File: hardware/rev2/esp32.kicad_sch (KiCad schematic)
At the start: 0 parts

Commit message: Begun ESP32 Power + Antenna
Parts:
- added C20: 10 uF, symbol Device:C
- added C21, C22, C24, C25, C26: 0,1 uF, symbol Device:C
- added C23, C27, C28: 1 uF, symbol Device:C
- added C29: 10 nF, symbol Device:C
- added C30, C31, C32, C33: TBD, symbol Device:C
- added L7: 2,0 nH (0,1 nH), symbol Device:L
- added L8, L9: TBD, symbol Device:L
- added U3: ESP32-S3, Package_DFN_QFN:QFN-56-1EP_7x7mm_P0.4mm_EP4x4mm, symbol MCU_Espressif:ESP32-S3
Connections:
- new net: C21.1, L7.2, U3.2 (VDD3P3), U3.3 (VDD3P3)
- new net: C31.1, C32.1, L8.1, L9.2
- new net: C30.1, L8.2, U3.1 (LNA_IN)
- new net Antenn (ESD mellan?): C33.1, L9.1
- new net BUSY: U3.18 (GPIO13)
- new net CS: U3.14 (GPIO9)
- new net DIO1: U3.17 (GPIO12)
- new net GND: C20.2, C21.2, C22.2, C23.2, C24.2, C25.2, C26.2, C27.2, C28.2, C29.2, C30.2, C31.2, C32.2, C33.2, U3.57 (GND)
- new net MISO: U3.12 (GPIO7)
- new net MOSI: U3.13 (GPIO8)
- new net Reset: U3.16 (GPIO11)
- new net SCK: U3.15 (GPIO10)
- new net VDD33: C20.1, C22.1, C23.1, C24.1, C25.1, C28.1, C29.1, L7.1, U3.20 (VDD3P3_RTC), U3.46 (VDD3P3_CPU), U3.55 (VDDA), U3.56 (VDDA)
- new net VDD_SPI: C26.1, C27.1, U3.29 (VDD_SPI)
- no-connect marks 0 -> 5

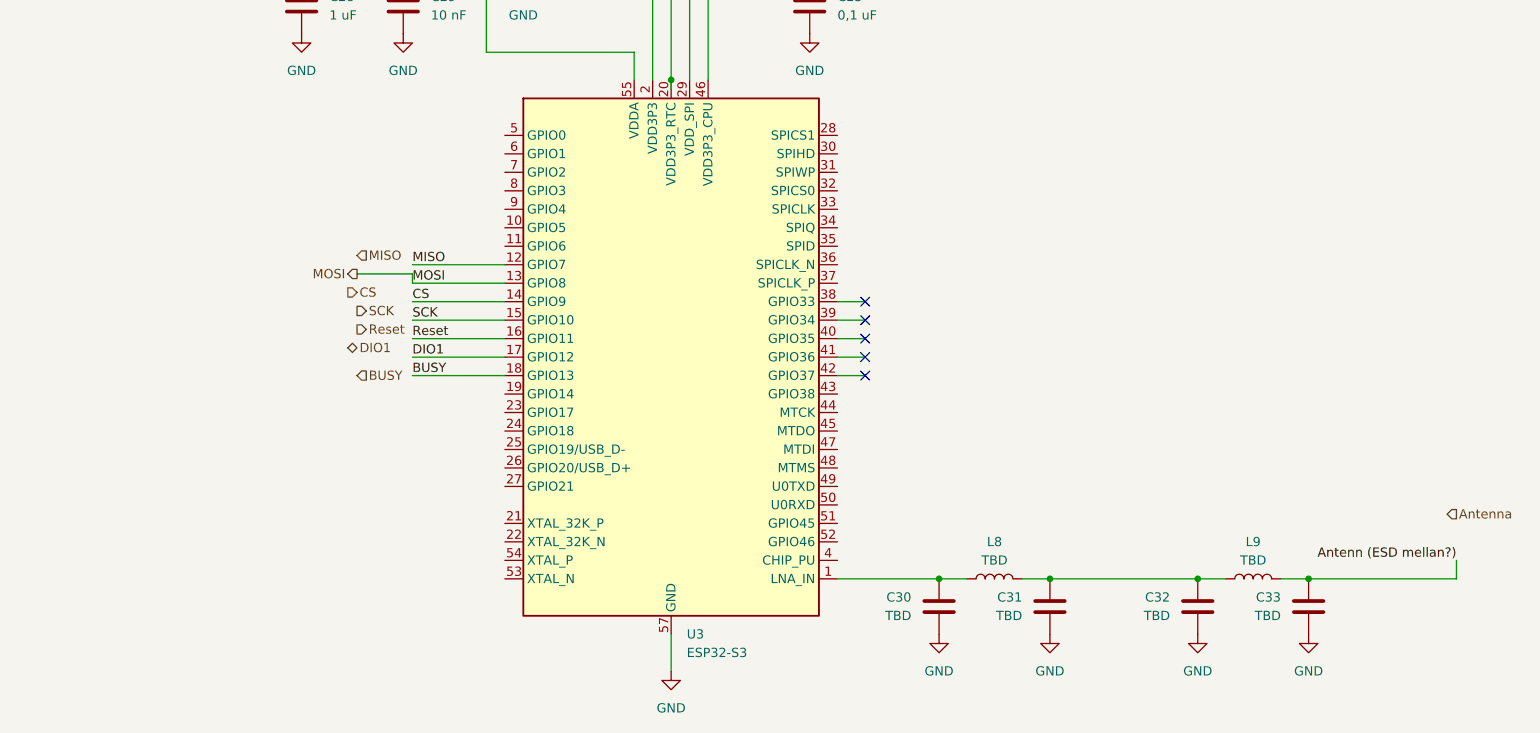
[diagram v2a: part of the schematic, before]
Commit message: added USB port to ESP32
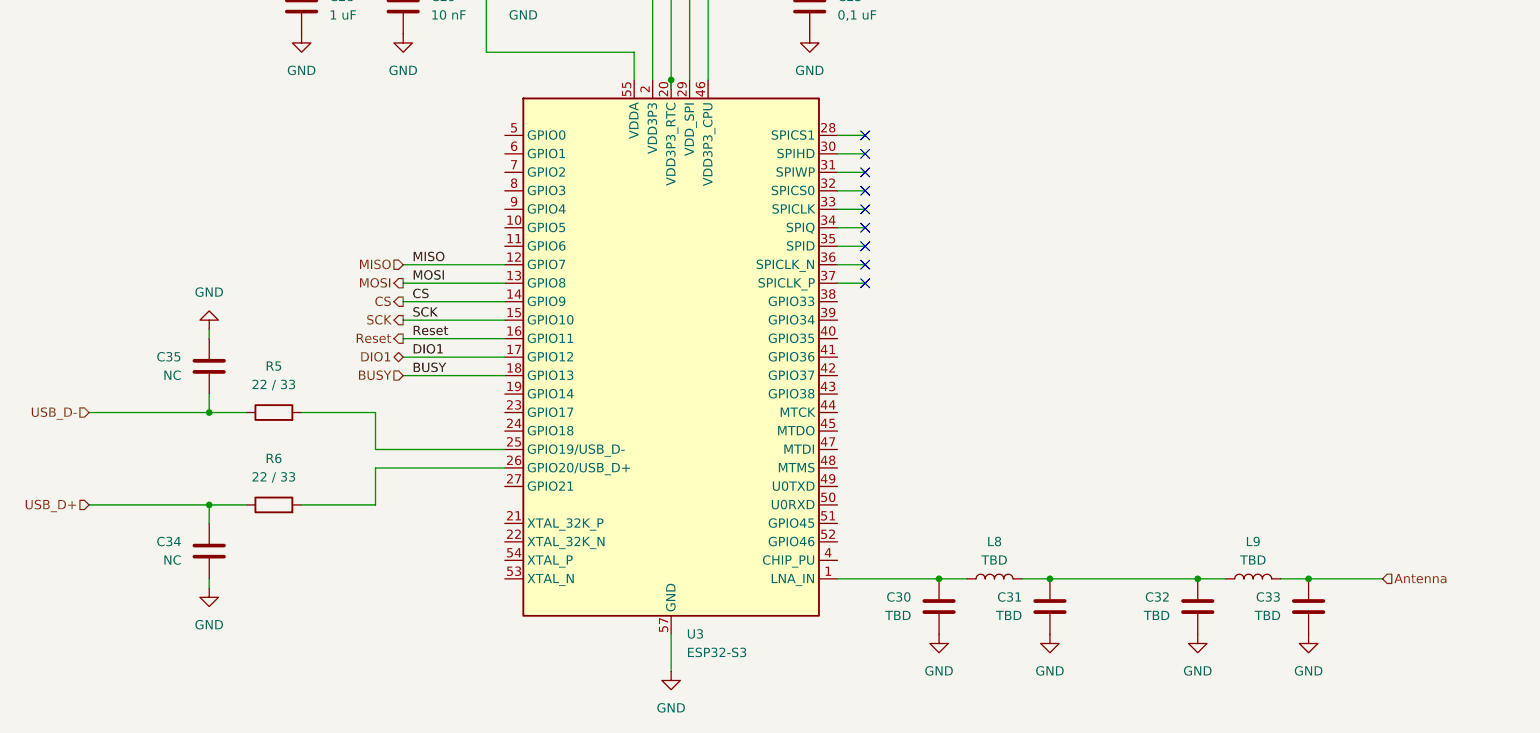
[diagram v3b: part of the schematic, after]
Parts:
- added C34, C35: NC, symbol Device:C
- added R5, R6: 22 / 33, symbol Device:R
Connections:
- net Antenn (ESD mellan?) is gone; now on net Antenna: C33.1, L9.1
- net GND: now also C34.2, C35.2
- net at U3.25 (GPIO19/USB_D-): now also R5.2
- net at U3.26 (GPIO20/USB_D+): now also R6.2
- new net USB_D+: C34.1, R6.1
- new net USB_D-: C35.1, R5.1
- no-connect marks 5 -> 9

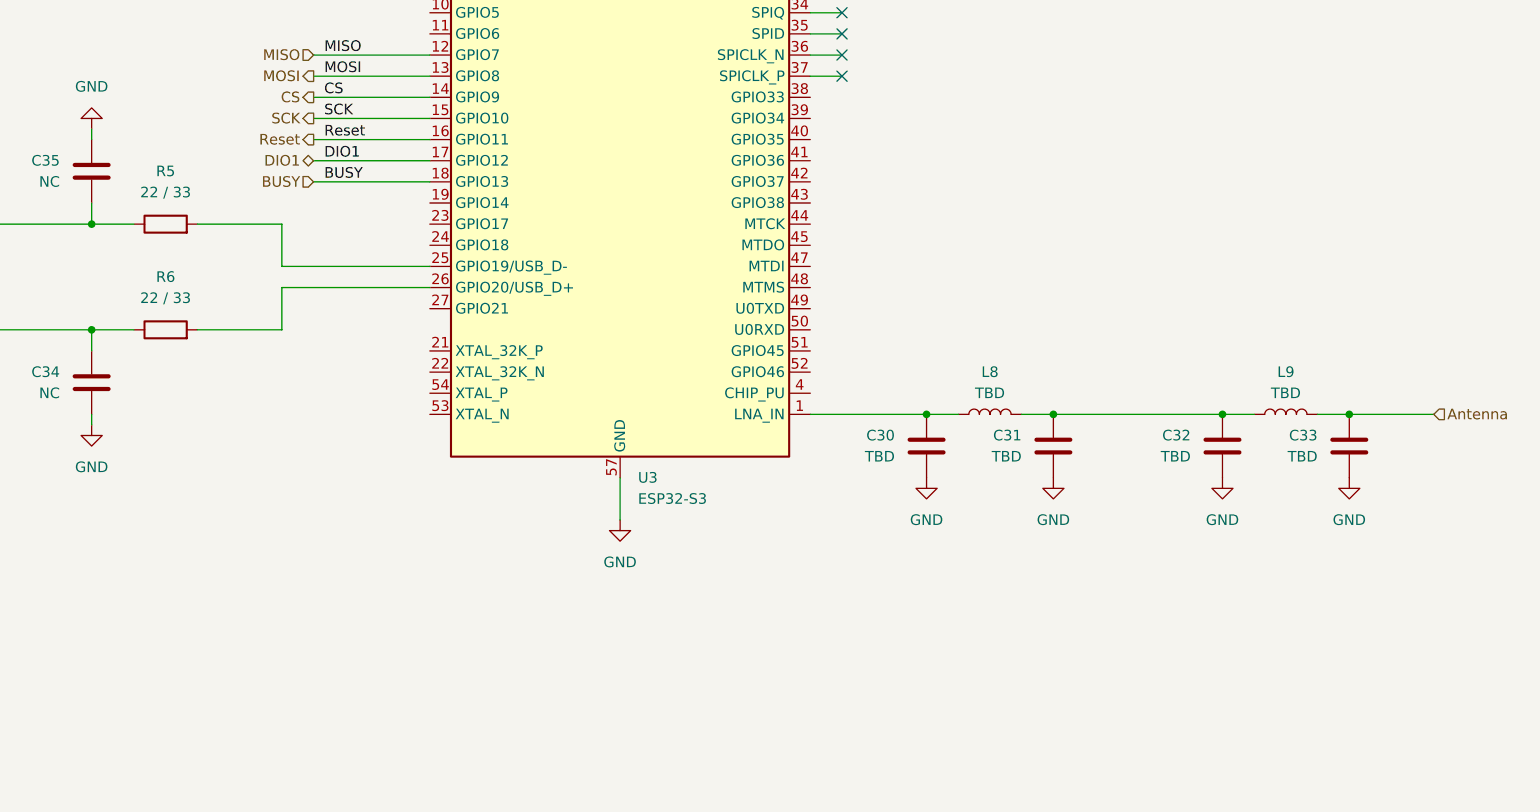
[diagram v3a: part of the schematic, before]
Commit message: Added XTAL and CHIP_PU
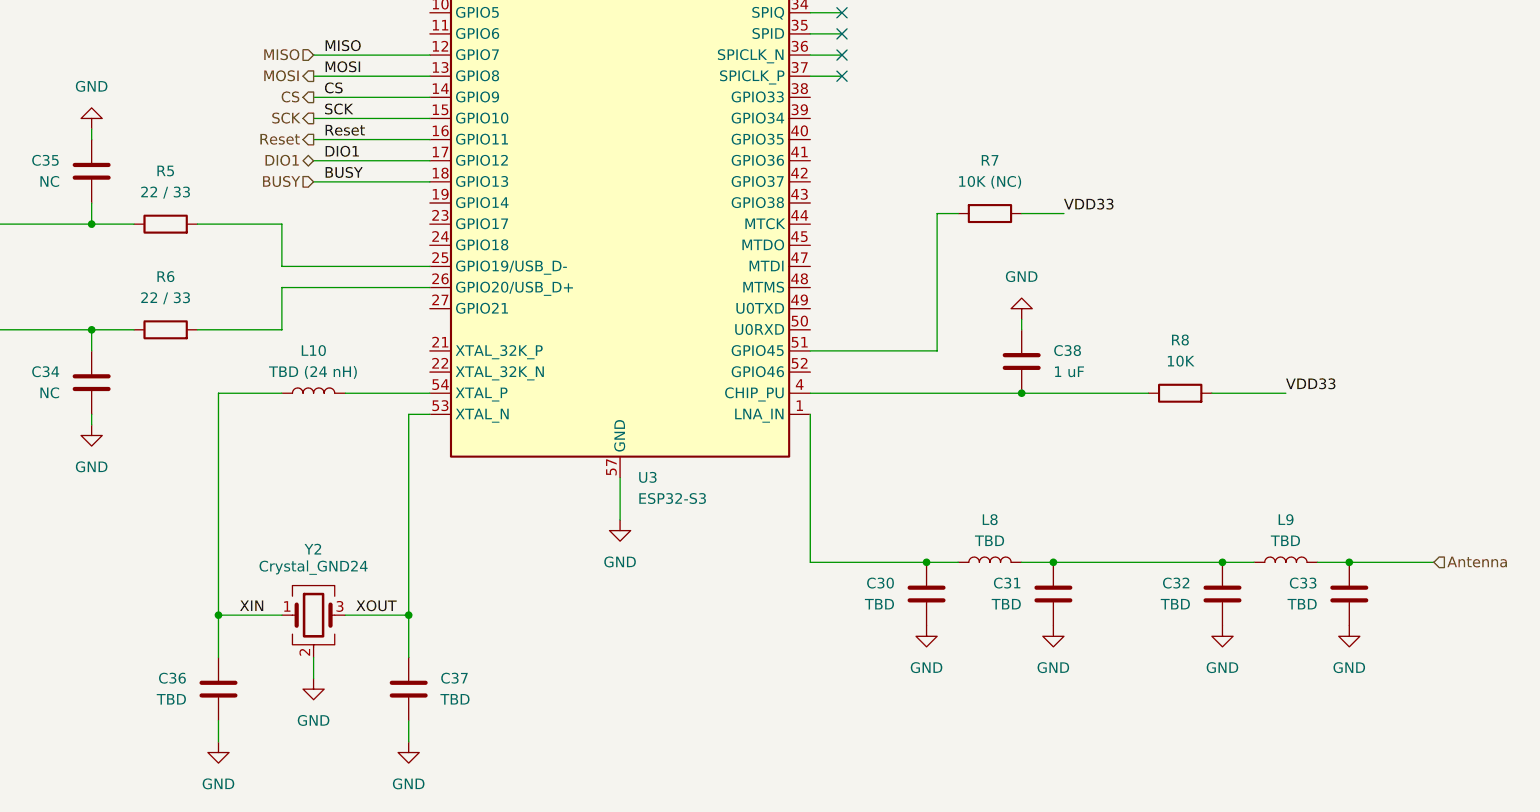
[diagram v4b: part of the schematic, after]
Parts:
- added C36, C37: TBD, symbol Device:C
- added C38: 1 uF, symbol Device:C
- added L10: TBD (24 nH), symbol Device:L
- added R7: 10K (NC), symbol Device:R
- added R8: 10K, symbol Device:R
- added Y2: Crystal_GND24, symbol Device:Crystal_GND24
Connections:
- net GND: now also C36.2, C37.2, C38.2, Y2.2 (G), Y2.4 (G)
- net VDD33: now also R7.1, R8.2
- net at U3.4 (CHIP_PU): now also C38.1, R8.1
- net at U3.51 (GPIO45): now also R7.2
- net XOUT: now reaches U3.53 (XTAL_N)
- net XOUT: now also C37.1, Y2.3
- net at U3.54 (XTAL_P): now also L10.2
- new net XIN: C36.1, L10.1, Y2.1
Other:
- moved on the sheet: C30, C31, C32, C33, L8, L9

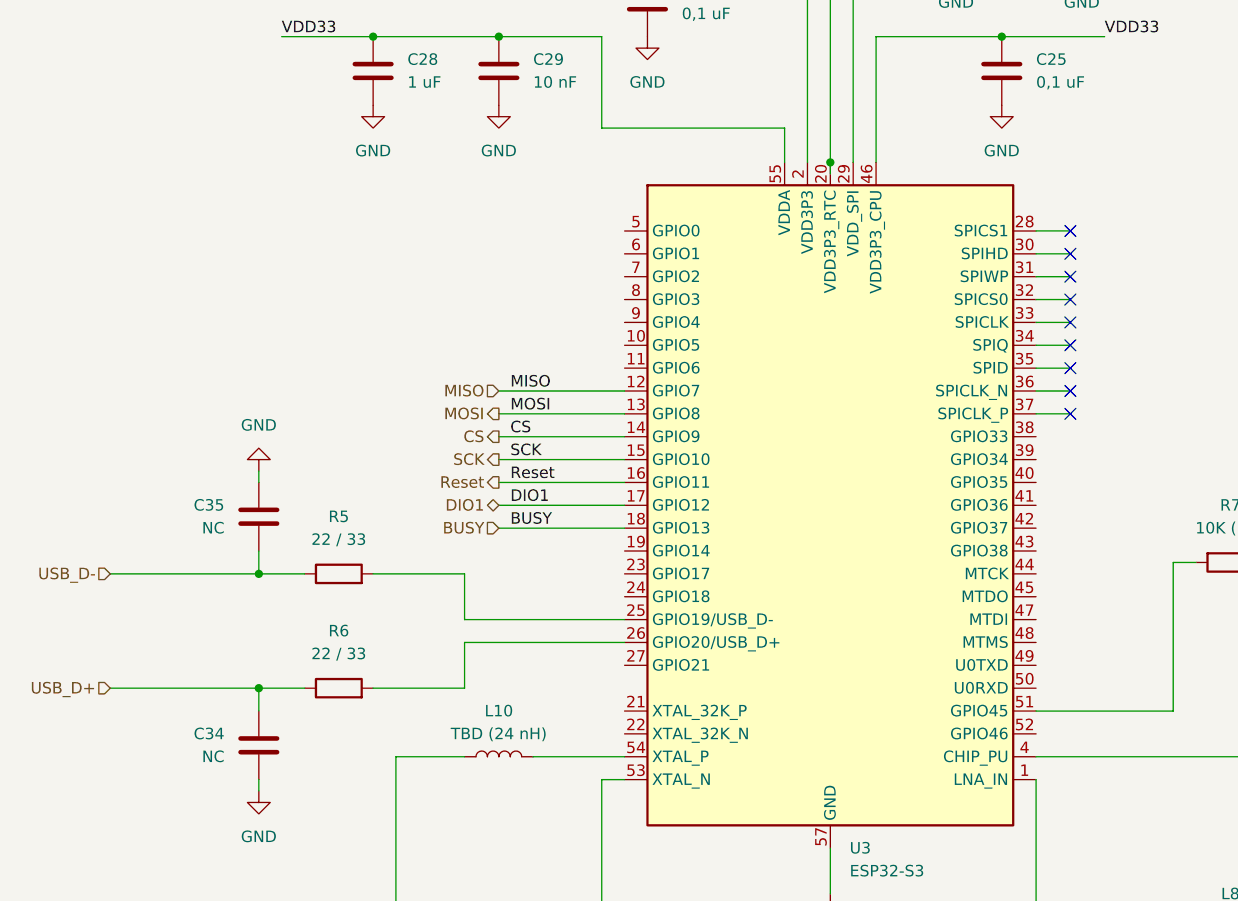
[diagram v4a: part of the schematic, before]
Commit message: Added NC pins and GPIO0
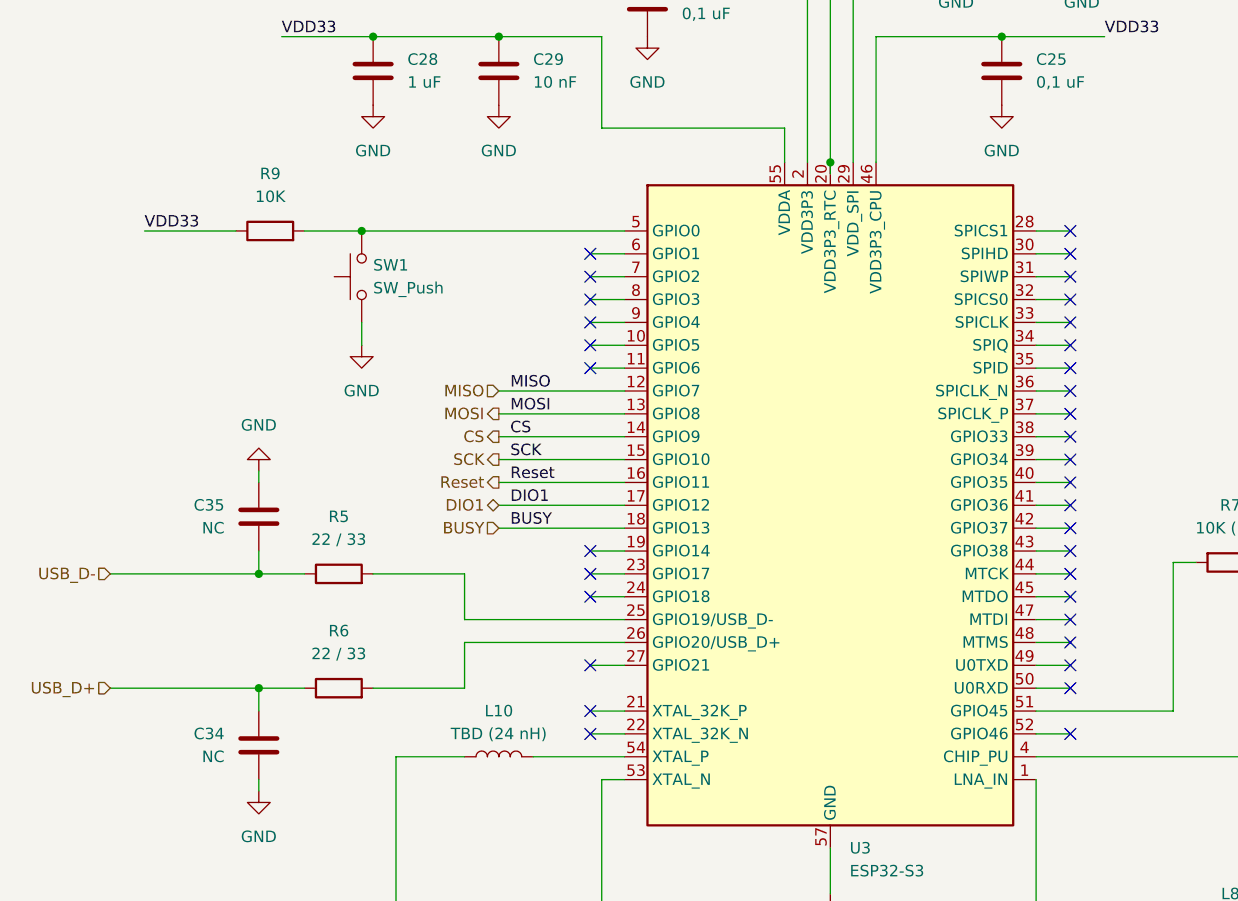
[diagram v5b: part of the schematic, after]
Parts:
- added R9: 10K, symbol Device:R
- added SW1: SW_Push, symbol Switch:SW_Push
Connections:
- net GND: now also SW1.1
- net VDD33: now also R9.1
- net at U3.5 (GPIO0): now also R9.2, SW1.2
- no-connect marks 9 -> 34
